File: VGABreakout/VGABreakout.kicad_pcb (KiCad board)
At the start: 2 copper layers, 67 x 91.3 mm, 12 parts, among them J1 DB15_Female_HighDensity, J2 Conn_01x02_Female, J3 Conn_01x05_Female, J4 Conn_01x05_Female, J5 DB15_Female_HighDensity, SW1 SW_SPST, SW2 SW_SPST, SW3 SW_SPST, SW4 SW_SPST, SW5 SW_SPST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

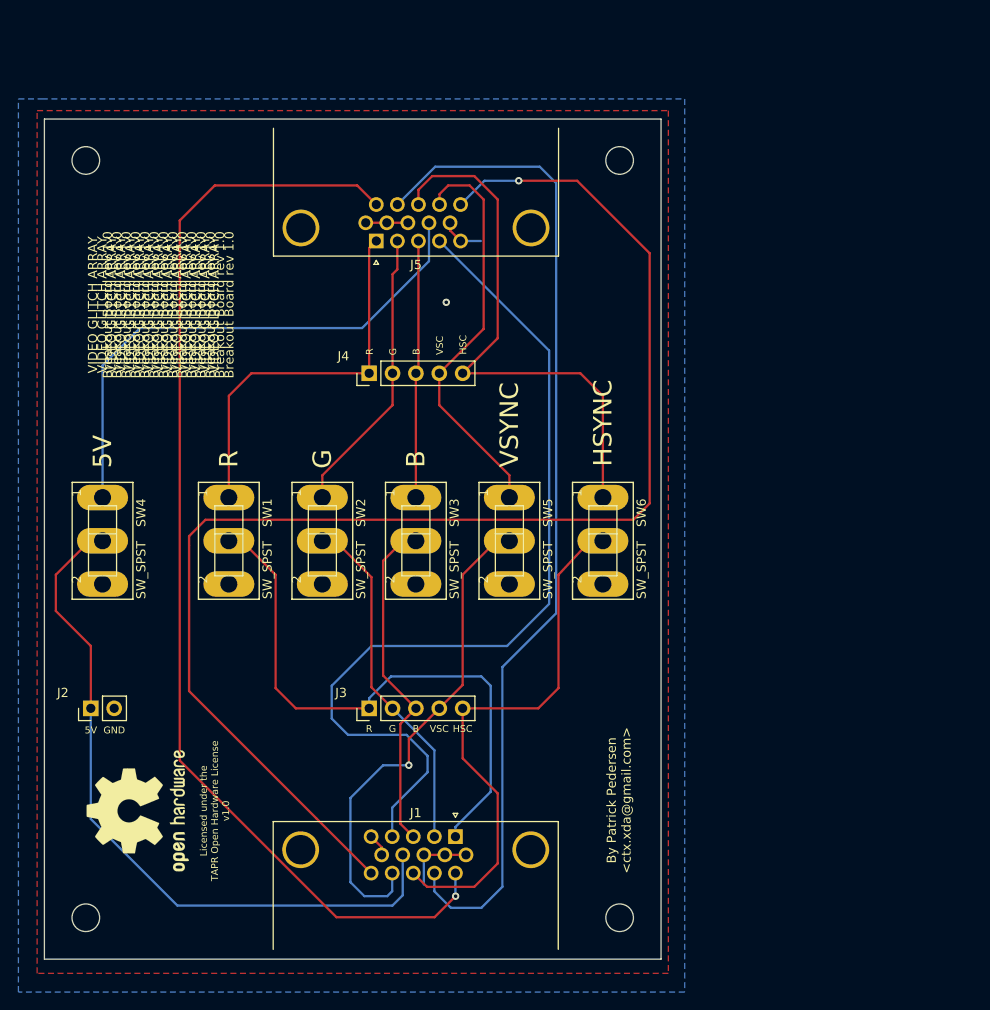
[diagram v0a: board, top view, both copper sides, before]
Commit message: VGABreakout: rev1.1:  Fixed text orientation and rotated board in pcbnew
Signed-off-by: Patrick Pedersen <ctx.xda@gmail.com>
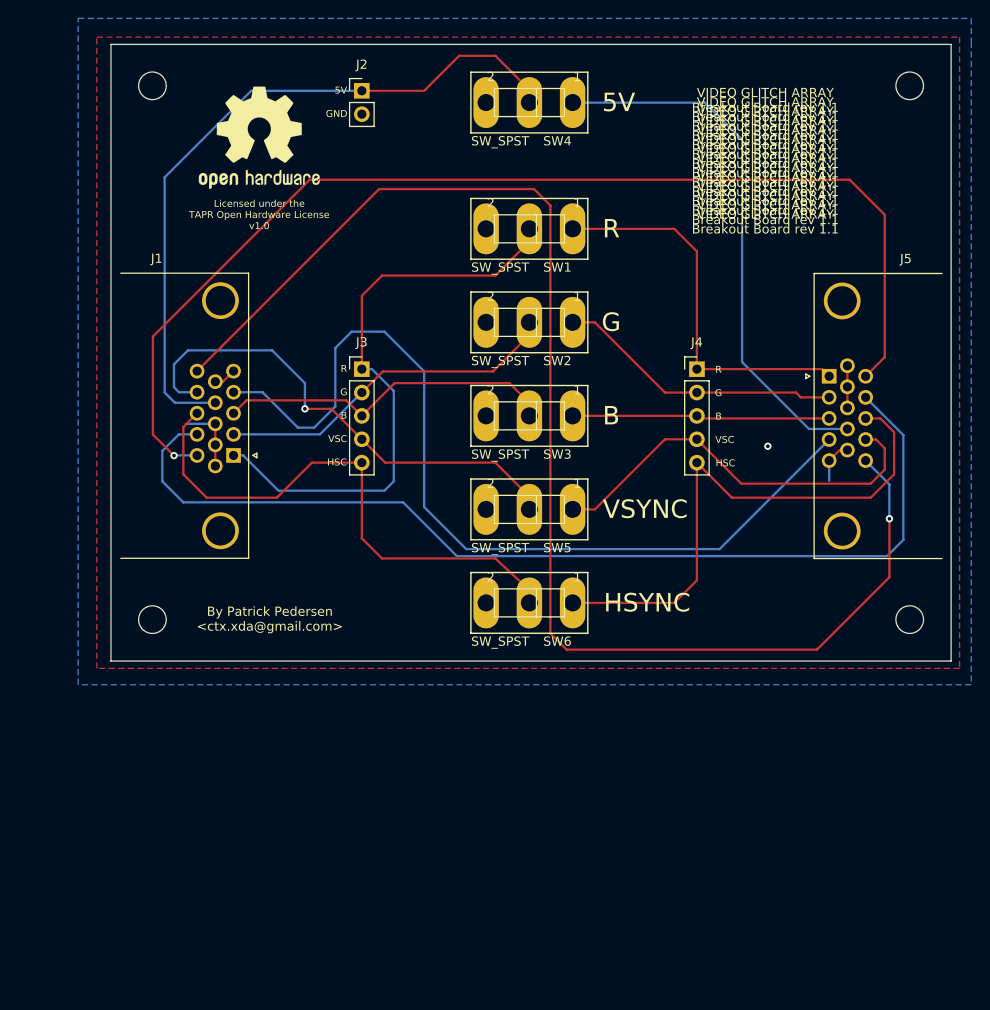
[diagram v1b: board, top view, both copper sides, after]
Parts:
- moved REF** 74.3 mm to (117.6, 69.2), turned to 0 degrees
- moved J2 73.3 mm to (128.8, 64.1), turned to 0 degrees
- moved SW4 66.5 mm to (147.0, 65.4), turned to 180 degrees
- moved J5 51.4 mm to (179.5, 95.2), turned to 90 degrees
- moved J1 47.9 mm to (114.8, 103.8), turned to 270 degrees
- moved SW1 47.1 mm to (147.0, 79.1), turned to 180 degrees
- moved J3 36.9 mm to (128.8, 94.4), turned to 0 degrees
- moved J4 35.6 mm to (165.2, 94.4), turned to 0 degrees
- moved SW2 32.7 mm to (147.0, 89.3), turned to 180 degrees
- moved SW3 18.3 mm to (147.0, 99.5), turned to 180 degrees
- moved SW6 10.5 mm to (147.0, 119.8), turned to 180 degrees
- moved SW5 4.05 mm to (147.0, 109.6), turned to 180 degrees
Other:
- board size 67 x 91.3 mm -> 91.3 x 67 mm
- board text added: "VIDEO GLITCH ARRAY Breakout Board rev 1.1"
- board text removed: "VIDEO GLITCH ARRAY Breakout Board rev 1.0"

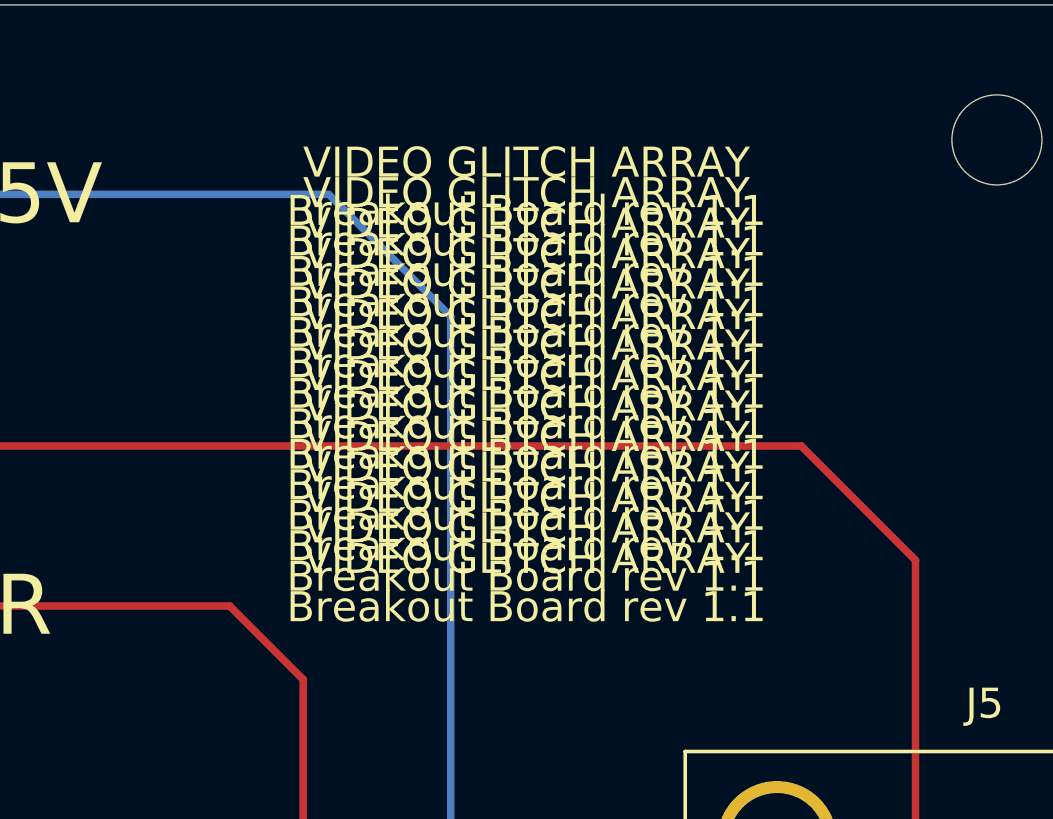
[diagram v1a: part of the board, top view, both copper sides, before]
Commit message: Updated PCB revisioning system to <SCHEM MAJOR>.<SCHEM MINOR>.<PCB>
Signed-off-by: Patrick Pedersen <ctx.xda@gmail.com>
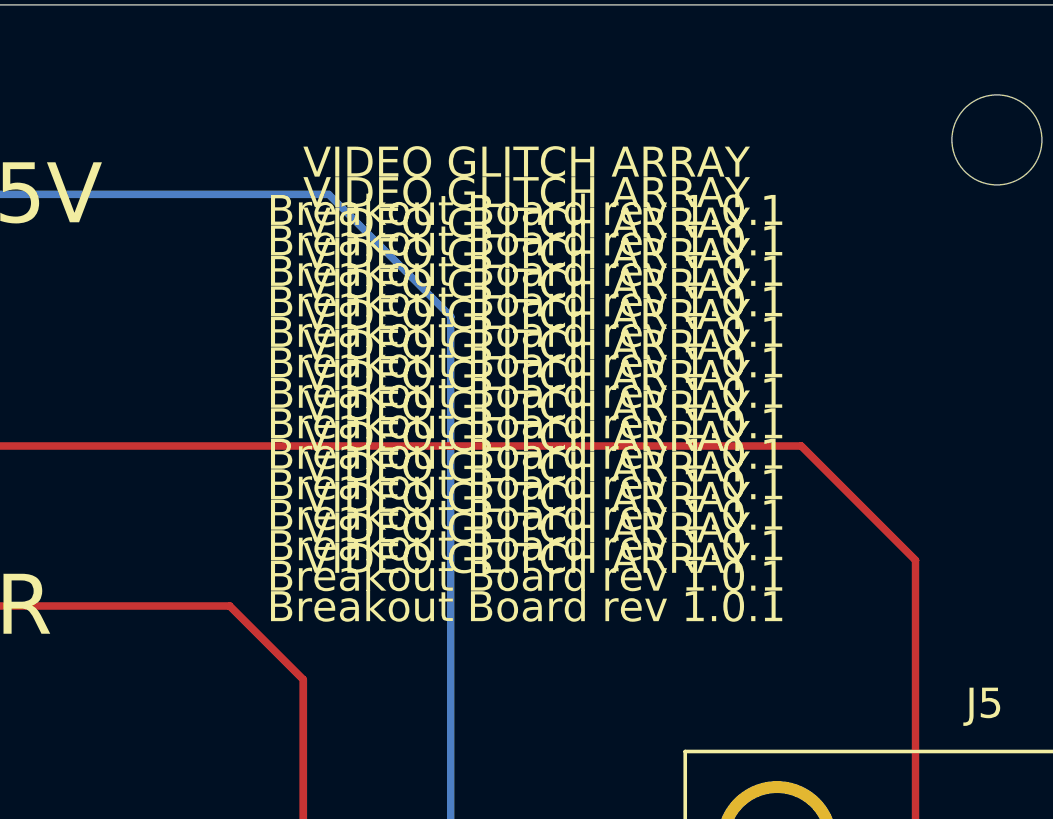
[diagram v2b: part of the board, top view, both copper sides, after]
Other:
- board text added: "VIDEO GLITCH ARRAY Breakout Board rev 1.0.1"
- board text removed: "VIDEO GLITCH ARRAY Breakout Board rev 1.1"
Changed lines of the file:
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@@
     (title "VIDEO GLITCH ARRAY Breakout")
     (date 2019-08-28)
-    (rev 1.1)
+    (rev 1.0.1)
     (comment 2 https://www.tapr.org/ohl.html)
     (comment 3 "License: TAPR Open Hardware License v1.0")
@@
     (effects (font (size 0.75 0.75) (thickness 0.1)))
   )
-  (gr_text "VIDEO GLITCH ARRAY\nBreakout Board rev 1.1" (at 172.591462 78.37424) (layer F.SilkS)
-    (effects (font (size 1 1) (thickness 0.15)))
-  )
-  (gr_text "VIDEO GLITCH ARRAY\nBreakout Board rev 1.1" (at 172.591462 77.35824) (layer F.SilkS)
-    (effects (font (size 1 1) (thickness 0.15)))
-  )
-  (gr_text "VIDEO GLITCH ARRAY\nBreakout Board rev 1.1" (at 172.591462 76.34224) (layer F.SilkS)
-    (effects (font (size 1 1) (thickness 0.15)))
-  )
-  (gr_text "VIDEO GLITCH ARRAY\nBreakout Board rev 1.1" (at 172.591462 75.32624) (layer F.SilkS)
-    (effects (font (size 1 1) (thickness 0.15)))
-  )
-  (gr_text "VIDEO GLITCH ARRAY\nBreakout Board rev 1.1" (at 172.591462 74.31024) (layer F.SilkS)
-    (effects (font (size 1 1) (thickness 0.15)))
-  )
-  (gr_text "VIDEO GLITCH ARRAY\nBreakout Board rev 1.1" (at 172.591462 73.29424) (layer F.SilkS)
-    (effects (font (size 1 1) (thickness 0.15)))
-  )
-  (gr_text "VIDEO GLITCH ARRAY\nBreakout Board rev 1.1" (at 172.591462 72.27824) (layer F.SilkS)
-    (effects (font (size 1 1) (thickness 0.15)))
-  )
-  (gr_text "VIDEO GLITCH ARRAY\nBreakout Board rev 1.1" (at 172.591462 71.26224) (layer F.SilkS)
-    (effects (font (size 1 1) (thickness 0.15)))
-  )
-  (gr_text "VIDEO GLITCH ARRAY\nBreakout Board rev 1.1" (at 172.591462 70.24624) (layer F.SilkS)
-    (effects (font (size 1 1) (thickness 0.15)))
-  )
-  (gr_text "VIDEO GLITCH ARRAY\nBreakout Board rev 1.1" (at 172.591462 69.23024) (layer F.SilkS)
-    (effects (font (size 1 1) (thickness 0.15)))
-  )
-  (gr_text "VIDEO GLITCH ARRAY\nBreakout Board rev 1.1" (at 172.591462 68.21424) (layer F.SilkS)
-    (effects (font (size 1 1) (thickness 0.15)))
-  )
-  (gr_text "VIDEO GLITCH ARRAY\nBreakout Board rev 1.1" (at 172.591462 67.19824) (layer F.SilkS)
-    (effects (font (size 1 1) (thickness 0.15)))
-  )
-  (gr_text "VIDEO GLITCH ARRAY\nBreakout Board rev 1.1" (at 172.591462 66.18224) (layer F.SilkS)
+  (gr_text "VIDEO GLITCH ARRAY\nBreakout Board rev 1.0.1" (at 172.591462 78.37424) (layer F.SilkS)
+    (effects (font (size 1 1) (thickness 0.15)))
+  )
+  (gr_text "VIDEO GLITCH ARRAY\nBreakout Board rev 1.0.1" (at 172.591462 77.35824) (layer F.SilkS)
+    (effects (font (size 1 1) (thickness 0.15)))
+  )
+  (gr_text "VIDEO GLITCH ARRAY\nBreakout Board rev 1.0.1" (at 172.591462 76.34224) (layer F.SilkS)
+    (effects (font (size 1 1) (thickness 0.15)))
+  )
+  (gr_text "VIDEO GLITCH ARRAY\nBreakout Board rev 1.0.1" (at 172.591462 75.32624) (layer F.SilkS)
+    (effects (font (size 1 1) (thickness 0.15)))
+  )
+  (gr_text "VIDEO GLITCH ARRAY\nBreakout Board rev 1.0.1" (at 172.591462 74.31024) (layer F.SilkS)
+    (effects (font (size 1 1) (thickness 0.15)))
+  )
+  (gr_text "VIDEO GLITCH ARRAY\nBreakout Board rev 1.0.1" (at 172.591462 73.29424) (layer F.SilkS)
+    (effects (font (size 1 1) (thickness 0.15)))
+  )
+  (gr_text "VIDEO GLITCH ARRAY\nBreakout Board rev 1.0.1" (at 172.591462 72.27824) (layer F.SilkS)
+    (effects (font (size 1 1) (thickness 0.15)))
+  )
+  (gr_text "VIDEO GLITCH ARRAY\nBreakout Board rev 1.0.1" (at 172.591462 71.26224) (layer F.SilkS)
+    (effects (font (size 1 1) (thickness 0.15)))
+  )
+  (gr_text "VIDEO GLITCH ARRAY\nBreakout Board rev 1.0.1" (at 172.591462 70.24624) (layer F.SilkS)
+    (effects (font (size 1 1) (thickness 0.15)))
+  )
+  (gr_text "VIDEO GLITCH ARRAY\nBreakout Board rev 1.0.1" (at 172.591462 69.23024) (layer F.SilkS)
+    (effects (font (size 1 1) (thickness 0.15)))
+  )
+  (gr_text "VIDEO GLITCH ARRAY\nBreakout Board rev 1.0.1" (at 172.591462 68.21424) (layer F.SilkS)
+    (effects (font (size 1 1) (thickness 0.15)))
+  )
+  (gr_text "VIDEO GLITCH ARRAY\nBreakout Board rev 1.0.1" (at 172.591462 67.19824) (layer F.SilkS)
+    (effects (font (size 1 1) (thickness 0.15)))
+  )
+  (gr_text "VIDEO GLITCH ARRAY\nBreakout Board rev 1.0.1" (at 172.591462 66.18224) (layer F.SilkS)
     (effects (font (size 1 1) (thickness 0.15)))
   )
@@
     (effects (font (size 0.75 0.75) (thickness 0.1)))
   )
-  (gr_text "VIDEO GLITCH ARRAY\nBreakout Board rev 1.1" (at 172.591462 65.16624) (layer F.SilkS)
-    (effects (font (size 1 1) (thickness 0.15)))
-  )
+  (gr_text "VIDEO GLITCH ARRAY\nBreakout Board rev 1.0.1" (at 172.591462 65.16624) (layer F.SilkS)
+    (effects (font (size 1 1) (thickness 0.15)))
+  )

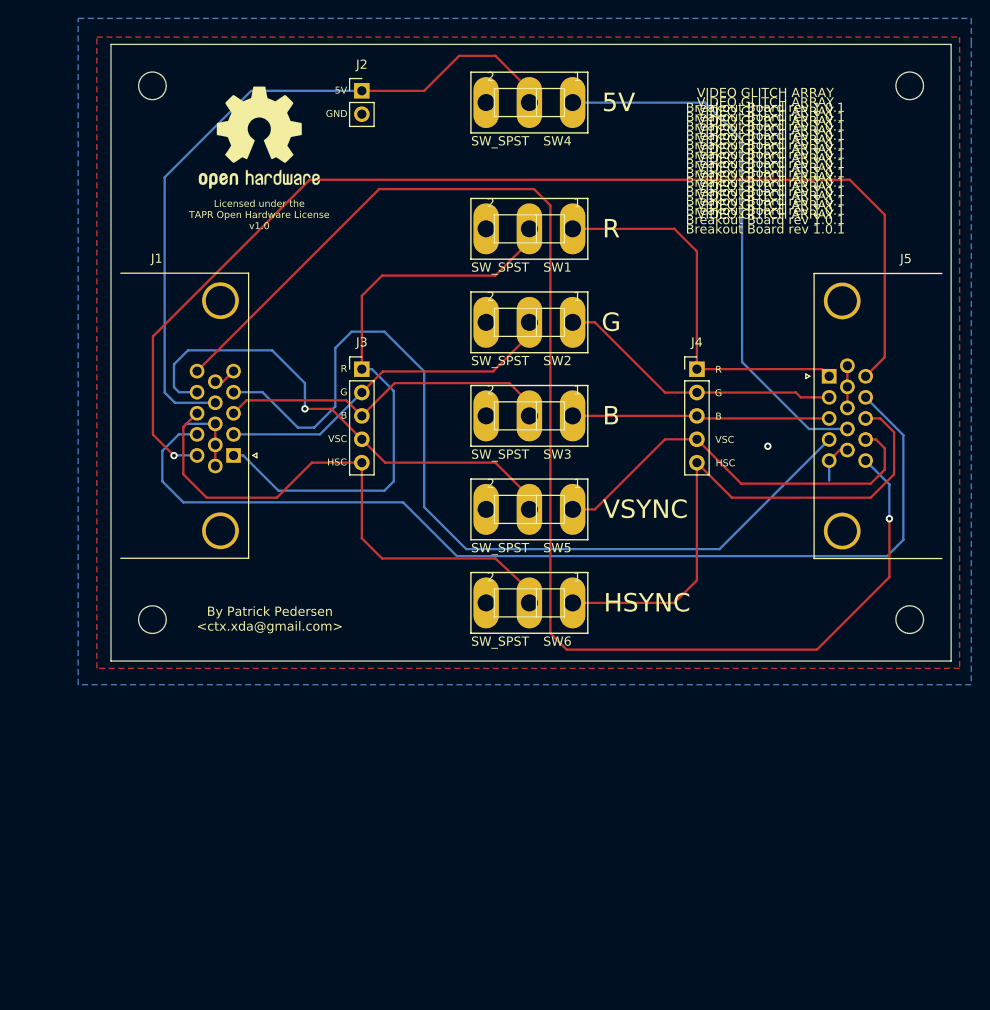
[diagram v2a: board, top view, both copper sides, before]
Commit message: VGABreakout: Rev 1.0.2: Fixed lables and trace irregularities/asymetries
Signed-off-by: Patrick Pedersen <ctx.xda@gmail.com>
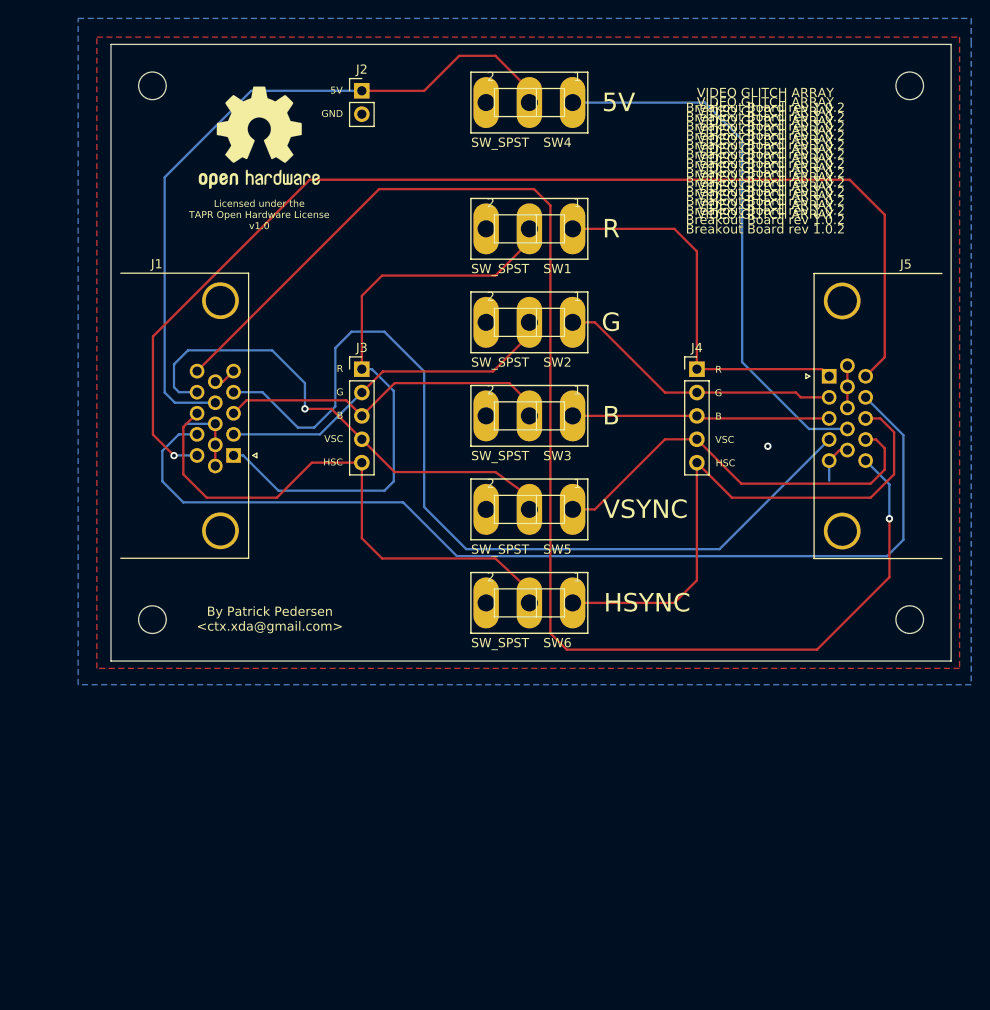
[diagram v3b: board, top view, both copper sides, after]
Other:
- board text added: "VIDEO GLITCH ARRAY Breakout Board rev 1.0.2"
- board text removed: "VIDEO GLITCH ARRAY Breakout Board rev 1.0.1"
